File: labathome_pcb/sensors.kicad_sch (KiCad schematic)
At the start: 30 parts, among them J16 BME280, J17 CCS811, J21 QWIIC, U12 BME680, U13 BME280, U15 CCS811, U19 DS18B20, U20 BH1750, U22 AM612, U23 MPU-6050, U26 MSM261D4030H1CPM, U3 AHT21, U7 DS18B20, X2 XGZP6897D

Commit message: Reorganization of code
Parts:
- removed C15, C28, C29, C30, C31, C37, C51, C52, C55: u1, Capacitor_SMD:C_0603_1608Metric, symbol Device:C
- removed C38: 1u, Capacitor_SMD:C_0603_1608Metric, symbol Device:C
- removed C39, C61: 10u, Capacitor_SMD:C_0603_1608Metric, symbol Device:C
- removed C50: 10n, Capacitor_SMD:C_0603_1608Metric, symbol Device:C
- removed C53: 2n2, Capacitor_SMD:C_0603_1608Metric, symbol Device:C
- removed J17: CCS811, Connector_PinSocket_2.54mm:PinSocket_1x08_P2.54mm_Vertical, symbol Connector_Generic:Conn_01x08
- removed J21: QWIIC, Connector_JST:JST_SH_SM04B-SRSS-TB_1x04-1MP_P1.00mm_Horizontal, symbol Connector_Generic:Conn_01x04
- removed R28: 4k7, Resistor_SMD:R_0603_1608Metric, symbol Device:R
- removed U12: BME680, Package_LGA:Bosch_LGA-8_3x3mm_P0.8mm_ClockwisePinNumbering, symbol Sensor:BME680
- removed U13: BME280, Package_LGA:Bosch_LGA-8_2.5x2.5mm_P0.65mm_ClockwisePinNumbering, symbol Sensor:BME280
- removed U15: CCS811, liebler_SEMICONDUCTORS:AMS_LGA-10-1EP_2.7x4mm_P0.6mm, symbol Sensor_Gas:CCS811
- removed U20: BH1750, liebler_MODULES:GY-302, symbol smopla:GY-302
- removed U23: MPU-6050, Sensor_Motion:InvenSense_QFN-24_4x4mm_P0.5mm, symbol Sensor_Motion:MPU-6050
- removed U26: MSM261D4030H1CPM, liebler_SEMICONDUCTORS:MSM261D4030H1CPM, symbol liebler_SEMICONDUCTORS:MSM261D4030H1CPM
- removed U3: AHT21, liebler_SEMICONDUCTORS:AHT21, symbol liebler_SEMICONDUCTORS:AHT21
- removed X2: XGZP6897D, liebler_MODULES:XGZP6897D, symbol liebler_MODULES:XGZP6897D
- added C54, C55 (x2), C57: u1, Capacitor_SMD:C_0201_0603Metric, symbol Device:C
- added C56: 22u, Capacitor_SMD:C_0603_1608Metric, symbol Device:C
- added J12: TCS34725, Connector_PinSocket_2.54mm:PinSocket_1x08_P2.54mm_Vertical, symbol Connector_Generic:Conn_01x08
- added J19: BH1750, Connector_PinSocket_2.54mm:PinSocket_1x06_P2.54mm_Vertical, symbol Connector_Generic:Conn_01x06
- added J20: CCS811, Connector_PinSocket_2.54mm:PinSocket_1x08_P2.54mm_Vertical, symbol Connector_Generic:Conn_01x08
- added J21: QWIIC, Connector_JST:JST_SH_SM04B-SRSS-TB_1x04-1MP_P1.00mm_Horizontal, symbol Connector_Generic_MountingPin:Conn_01x04_MountingPin
- added J23: VL53L5x, Connector_PinSocket_2.54mm:PinSocket_1x06_P2.54mm_Vertical, symbol Connector_Generic:Conn_01x06
- added J4: SCD4x, Connector_PinSocket_2.54mm:PinSocket_1x04_P2.54mm_Vertical, symbol Connector_Generic:Conn_01x04
- added R11: 10k, Resistor_SMD:R_0201_0603Metric, symbol Device:R
- added R9: k22, Resistor_SMD:R_0402_1005Metric, symbol Device:R
- added R9: GL5516, OptoDevice:R_LDR_5.1x4.3mm_P3.4mm_Vertical, symbol Device:R_Photo
- added U12: AHT20, liebler_SEMICONDUCTORS:AHT21, symbol liebler_SEMICONDUCTORS:AHT21
- added U9: LSM6DS3, Package_LGA:LGA-14_3x2.5mm_P0.5mm_LayoutBorder3x4y, symbol Sensor_Motion:LSM6DS3
- J16: value BME280 -> BMEx80
- R54: value 1M -> M1; footprint Resistor_SMD:R_0603_1608Metric -> Resistor_SMD:R_0201_0603Metric
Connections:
- net +3V3: now also C54.2, C55.2, C55.2, J12.5 (Pin_5), J19.5 (Pin_5), J20.1 (Pin_1), J21.2 (Pin_2), J23.1 (Pin_1), J4.2 (Pin_2), R9.1, R9.1, U9.12 (CS), U9.5 (VDDIO), U9.8 (VDD)
- net GND: now also C54.1, C55.1, C55.1, C56.2, C57.1, J12.6 (Pin_6), J19.1 (Pin_1), J19.4 (Pin_4), J20.2 (Pin_2), J20.5 (Pin_5), J21.1 (Pin_1), J21.MP (MountPin), J23.2 (Pin_2), J4.1 (Pin_1), R11.2, U12.5 (GND), U9.1 (SDO/SA0), U9.2 (SDX), U9.3 (SCX), U9.6 (GND), U9.7 (GND)
- net SCL: now also J12.4 (Pin_4), J19.3 (Pin_3), J20.3 (Pin_3), J21.4 (Pin_4), J23.3 (Pin_3), J4.3 (Pin_3), U12.3 (SCL), U9.13 (SCL)
- net SDA: now also J12.3 (Pin_3), J19.2 (Pin_2), J20.4 (Pin_4), J21.3 (Pin_3), J23.4 (Pin_4), J4.4 (Pin_4), U12.4 (SDA), U9.14 (SDA)
- new net: C56.1, C57.2, R9.2, U12.2 (VDD)
- new net BRIGHTNESS: R11.1, R9.2
- new net I2C_IRQ: J12.2 (Pin_2), J20.6 (Pin_6), J23.5 (Pin_5), U9.4 (INT1)
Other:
- note added: "6DOF-Sensor"
- note added: "Brightnerss (LDR)"
- note added: "CCS811"
- note added: "CS"
- note added: "Movement (PIR)"
- note added: "QWIIC"
- note added: "SDO"
- note added: "Temperature + Humidity"
- note added: "Temperature + Humidity (Alternative)"
- note added: "https://cdn.sparkfun.com/assets/2/4/7/e/6/SparkFun_Qwiic_Adapter.pdf"
- note removed: "7bit-ADDR=0x76"
- note removed: "According to https://cdn.sparkfun.com/assets/2/4/7/e/6/SparkFun_Qwiic_Adapter.pdf"
- note removed: "CSB=3V -> I2C"
- note removed: "OnBoard I2C"
- company: (none) -> Klaus Liebler
- title: (none) -> lab@home

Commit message: Bus servos
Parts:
- J23: value VL53L5x -> VL53L0x
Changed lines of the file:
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@@
 			)
 		)
-		(property "Value" "VL53L5x"
+		(property "Value" "VL53L0x"
 			(at 138.43 24.1299 0)
 			(effects

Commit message: Minor changes
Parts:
- C54, C55, C57: MPN (none) -> GRM033R61A104KE15D; Manufacturer (none) -> Murata Electronics
- C56: MPN (none) -> CL10A226MP8NUNE; Manufacturer (none) -> Samsung Electro-Mechanics
- J12, J20: MPN (none) -> 2.54-1*8P; Manufacturer (none) -> BOOMELE(Boom Precision Elec)
- J16, J19, J23: MPN (none) -> 2.54-1*6P; Manufacturer (none) -> BOOMELE(Boom Precision Elec)
- J21: MPN (none) -> SM04B-SRSS-TB(LF)(SN); Manufacturer (none) -> JST
- J4: MPN (none) -> 2.54-1*4P; Manufacturer (none) -> BOOMELE(Boom Precision Elec)
- R11: MPN (none) -> 0201WMF1002TEE; Manufacturer (none) -> UNI-ROYAL(Uniroyal Elec)
- R54: MPN (none) -> 0201WMF1003TEE; Manufacturer (none) -> UNI-ROYAL(Uniroyal Elec)
- R9: MPN (none) -> 0402WGF2200TCE; Manufacturer (none) -> UNI-ROYAL(Uniroyal Elec)
- R9: MPN (none) -> GL5516; Manufacturer (none) -> Senba Sensing Tech
- U12: MPN (none) -> AHT20; Manufacturer (none) -> Aosong (Guangzhou) Elec
- U19, U7: MPN (none) -> DS18B20; Manufacturer (none) -> MSKSEMI
- U22: MPN (none) -> BS612; Manufacturer (none) -> Senba Sensing Tech
- U9: MPN (none) -> LSM6DS3TR-C; Manufacturer (none) -> STMicroelectronics

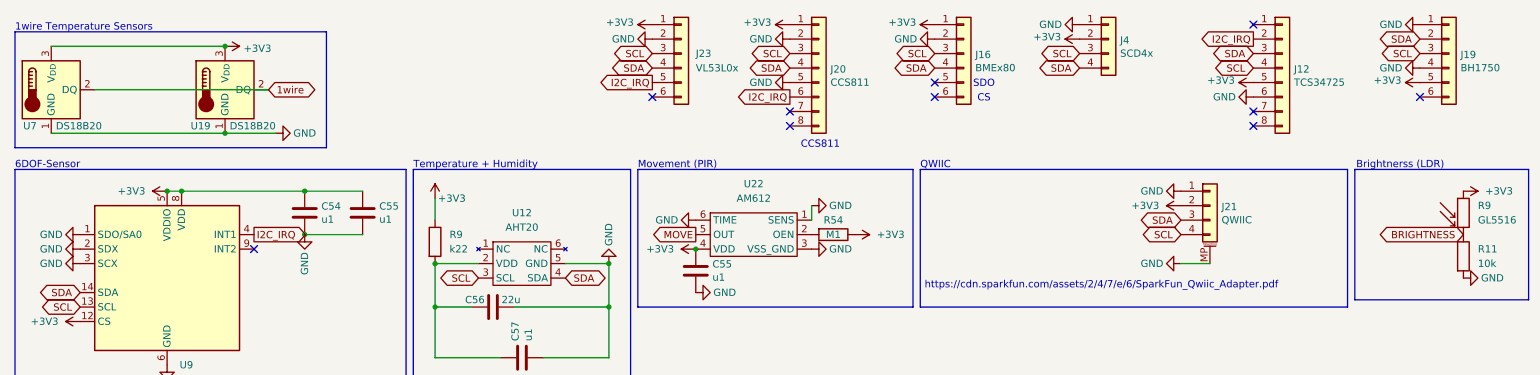
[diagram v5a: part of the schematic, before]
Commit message: Labathome PCB -> KICAD 9
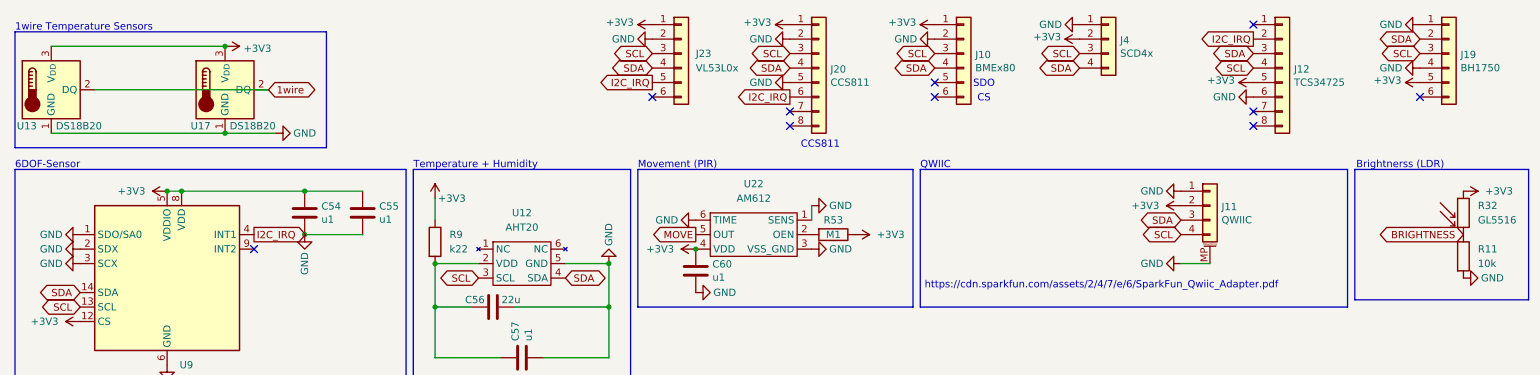
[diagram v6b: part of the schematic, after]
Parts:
- renumbered C55 to C60, J16 to J10, J21 to J11, R9 to R32, R54 to R53, U7 to U13, U19 to U17
